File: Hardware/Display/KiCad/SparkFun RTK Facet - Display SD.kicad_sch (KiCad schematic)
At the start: 27 parts, among them J1 Conn_01x12_FPC_0.5mm, J2 microSD, J3 I2C, J4 Conn_01x06_FPC_1.0mm, SW1 SMD_5.2x5.2mm_h2.5mm, U1 SSD1306

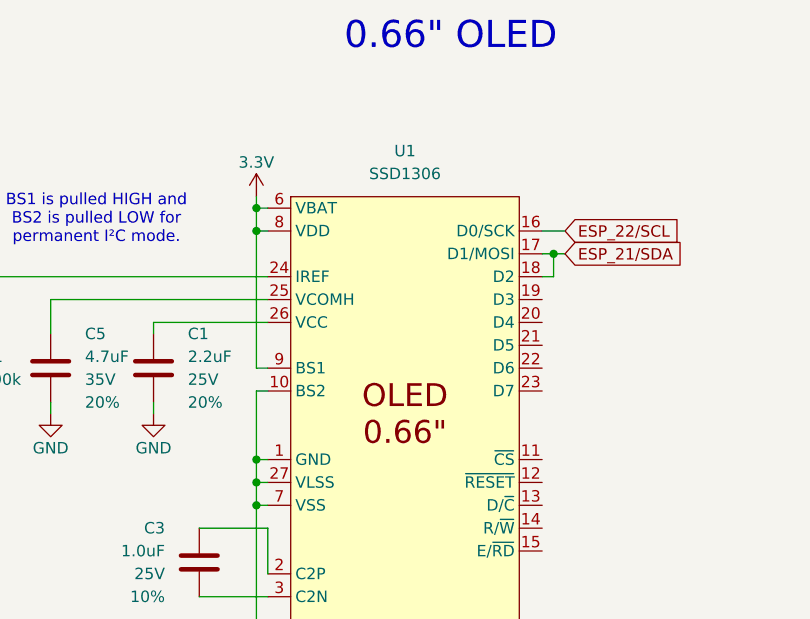
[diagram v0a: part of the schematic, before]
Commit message: Fix part number on LIF
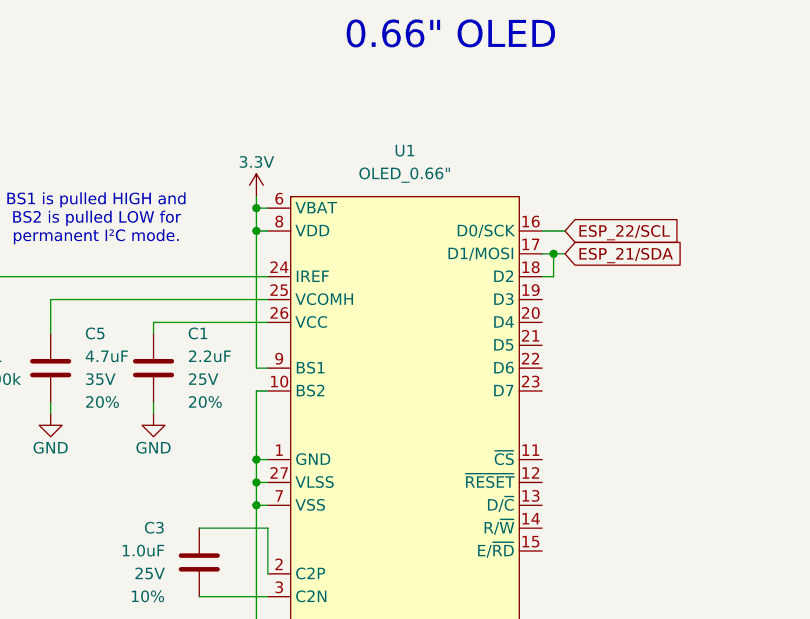
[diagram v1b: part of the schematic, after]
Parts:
- D1: footprint SparkFun-LED:LED_1206-Bottom -> SparkFun-LED:LED_1206_Bottom_Green
- J4: PROD_ID CONN-08971 -> CONN-16692
- SW1: Mfg Part# 8-004 SMD Button 8x3.6mm Height=2.5mm -> (none)
- U1: value SSD1306 -> OLED_0.66"; footprint SparkFun RTK Facet - Display SD:OLED-0.66-64X48-TRIM -> SparkFun-Display:OLED_0.66-SMD
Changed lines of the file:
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@@
 			)
 		)
-		(property "Footprint" "SparkFun-LED:LED_1206-Bottom"
+		(property "Footprint" "SparkFun-LED:LED_1206_Bottom_Green"
 			(at 100.33 153.67 0)
 			(effects
@@
 			)
 		)
-		(property "Datasheet" "https://datasheet.lcsc.com/lcsc/2110151630_XKB-Connectivity-XKTF-015-N_C381082.pdf"
+		(property "Datasheet" "https://cdn.sparkfun.com/assets/a/d/6/0/8/microSD_Datasheet_msd-1-a.pdf"
 			(at 220.98 85.09 0)
 			(effects
@@
 			)
 		)
-		(property "Value" "SSD1306"
+		(property "Value" "OLED_0.66\""
 			(at 125.73 34.29 0)
 			(effects
@@
 			)
 		)
-		(property "Footprint" "SparkFun RTK Facet - Display SD:OLED-0.66-64X48-TRIM"
+		(property "Footprint" "SparkFun-Display:OLED_0.66-SMD"
 			(at 125.73 95.25 0)
 			(effects
@@
 			)
 		)
-		(property "Description" "OLED display 0.66\" view area"
+		(property "Description" "OLED display 0.66\" view area 64x48 pixels"
 			(at 127 97.79 0)
 			(effects
@@
 			)
 		)
-		(property "Mfg Part#" "8-004 SMD Button 8x3.6mm Height=2.5mm"
-			(at 168.91 153.67 0)
-			(effects
-				(font
-					(size 1.27 1.27)
-				)
-				(hide yes)
-			)
-		)
 		(pin "2"
 		)
@@
 			)
 		)
-		(property "PROD_ID" "CONN-08971"
+		(property "PROD_ID" "CONN-16692"
 			(at 144.78 157.48 0)
 			(effects
